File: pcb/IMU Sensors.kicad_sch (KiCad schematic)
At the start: 15 parts, among them U4 MS5607-02BA, U5 LSM6DSL

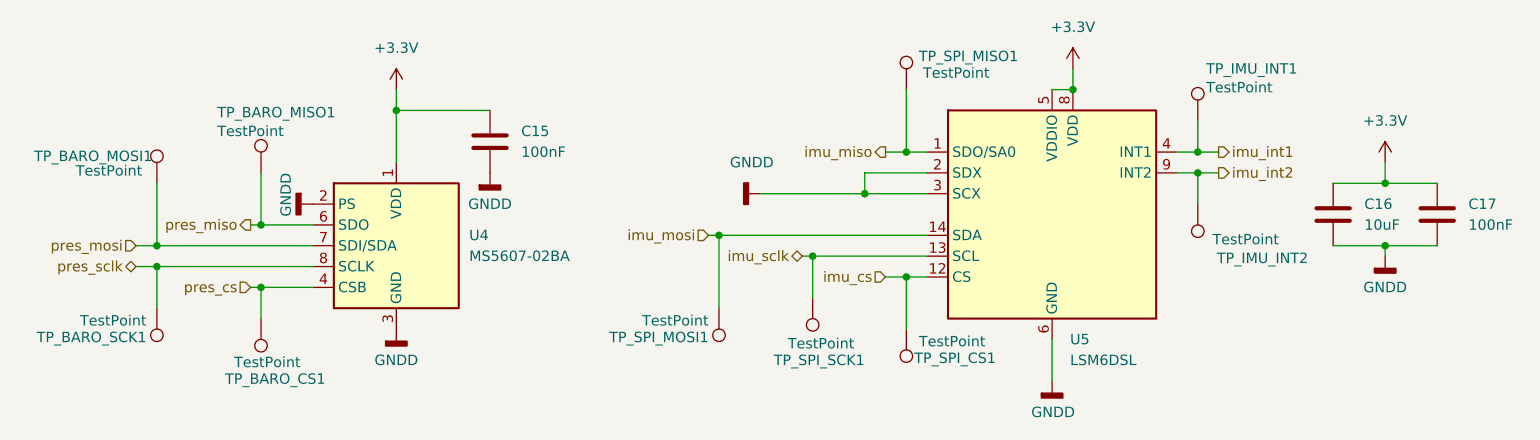
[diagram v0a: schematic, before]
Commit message: Updated schematics and removed most test points
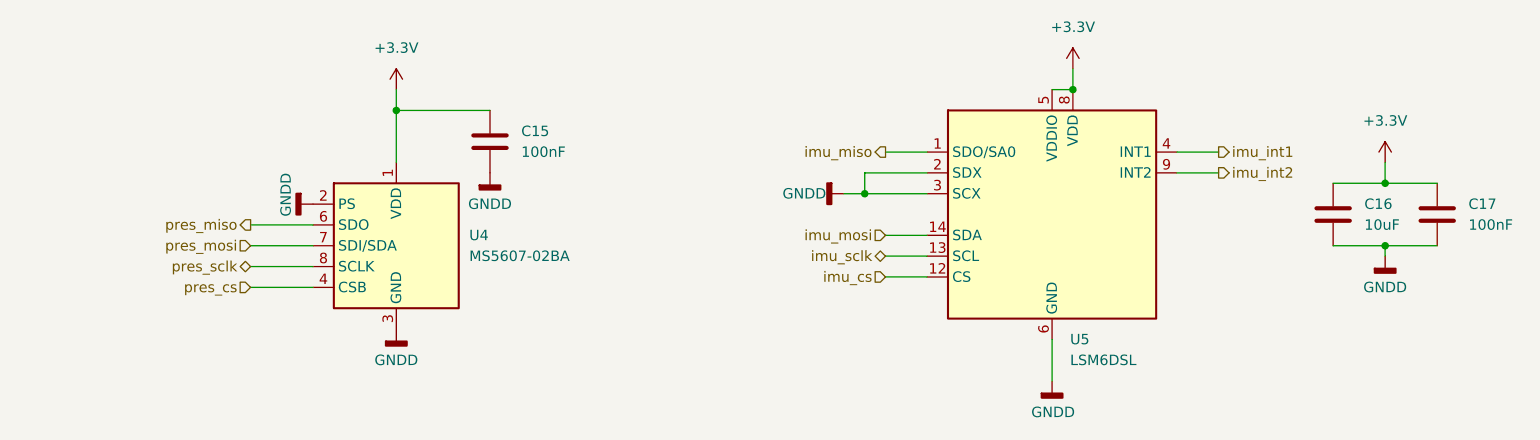
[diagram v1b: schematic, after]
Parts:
- removed TP_BARO_CS1, TP_BARO_MISO1, TP_BARO_MOSI1, TP_BARO_SCK1, TP_IMU_INT1, TP_IMU_INT2, TP_SPI_CS1, TP_SPI_MISO1, TP_SPI_MOSI1, TP_SPI_SCK1: TestPoint, TestPoint:TestPoint_Loop_D2.54mm_Drill1.5mm_Beaded, symbol Connector:TestPoint
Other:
- title: Ride-Along Module -> Control Module Rev2
